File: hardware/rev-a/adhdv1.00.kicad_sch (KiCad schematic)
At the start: 0 parts

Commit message: Create power and MCU hierarchal pages
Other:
- added sheet MCU (mcu.kicad_sch)
- added sheet power (power.kicad_sch)
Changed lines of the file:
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@@
 	(generator_version "9.0")
 	(paper "A4")
+	(wire
+		(pts
+			(xy 135.89 38.1) (xy 135.89 39.37)
+		)
+		(stroke
+			(width 0)
+			(type default)
+		)
+	)
+	(sheet
+		(at 233.68 26.67)
+		(size 45.72 54.61)
+		(exclude_from_sim no)
+		(in_bom yes)
+		(on_board yes)
+		(dnp no)
+		(fields_autoplaced yes)
+		(stroke
+			(width 0.1524)
+			(type solid)
+		)
+		(fill
+			(color 0 0 0 0.0000)
+		)
+		(property "Sheetname" "MCU"
+			(at 233.68 25.9584 0)
+			(effects
+				(font
+					(size 1.27 1.27)
+				)
+				(justify left bottom)
+			)
+		)
+		(property "Sheetfile" "mcu.kicad_sch"
+			(at 233.68 81.8646 0)
+			(effects
+				(font
+					(size 1.27 1.27)
+				)
+				(justify left top)
+			)
+		)
+		(pin "GND" passive
+			(at 233.68 69.85 180)
+			(effects
+				(font
+					(size 1.27 1.27)
+				)
+				(justify left)
+			)
+		)
+		(pin "CHG_STAT" input
+			(at 233.68 43.18 180)
+			(effects
+				(font
+					(size 1.27 1.27)
+				)
+				(justify left)
+			)
+		)
+		(pin "3V3" input
+			(at 233.68 49.53 180)
+			(effects
+				(font
+					(size 1.27 1.27)
+				)
+				(justify left)
+			)
+		)
+		(pin "PGOOD_STAT" input
+			(at 233.68 57.15 180)
+			(effects
+				(font
+					(size 1.27 1.27)
+				)
+				(justify left)
+			)
+		)
+		(pin "VBAT_ADC" input
+			(at 233.68 36.83 180)
+			(effects
+				(font
+					(size 1.27 1.27)
+				)
+				(justify left)
+			)
+		)
+		(instances
+			(project "adhdv1.00"
+				(path "/13efd387-de04-4584-baa5-02298cbea49f"
+					(page "3")
+				)
+			)
+		)
+	)
+	(sheet
+		(at 135.89 26.67)
+		(size 90.17 54.61)
+		(exclude_from_sim no)
+		(in_bom yes)
+		(on_board yes)
+		(dnp no)
+		(fields_autoplaced yes)
+		(stroke
+			(width 0.1524)
+			(type solid)
+		)
+		(fill
+			(color 0 0 0 0.0000)
+		)
+		(property "Sheetname" "power"
+			(at 135.89 25.9584 0)
+			(effects
+				(font
+					(size 1.27 1.27)
+				)
+				(justify left bottom)
+			)
+		)
+		(property "Sheetfile" "power.kicad_sch"
+			(at 135.89 81.8646 0)
+			(effects
+				(font
+					(size 1.27 1.27)
+				)
+				(justify left top)
+			)
+		)
+		(pin "3V3" output
+			(at 226.06 49.53 0)
+			(effects
+				(font
+					(size 1.27 1.27)
+				)
+				(justify right)
+			)
+		)
+		(pin "GND" passive
+			(at 226.06 69.85 0)
+			(effects
+				(font
+					(size 1.27 1.27)
+				)
+				(justify right)
+			)
+		)
+		(pin "USB_5V" input
+			(at 135.89 39.37 180)
+			(effects
+				(font
+					(size 1.27 1.27)
+				)
+				(justify left)
+			)
+		)
+		(pin "VBAT" output
+			(at 135.89 58.42 180)
+			(effects
+				(font
+					(size 1.27 1.27)
+				)
+				(justify left)
+			)
+		)
+		(pin "VBAT_ADC" output
+			(at 226.06 36.83 0)
+			(effects
+				(font
+					(size 1.27 1.27)
+				)
+				(justify right)
+			)
+		)
+		(pin "CHG_STAT" output
+			(at 226.06 43.18 0)
+			(effects
+				(font
+					(size 1.27 1.27)
+				)
+				(justify right)
+			)
+		)
+		(pin "PGOOD_STAT" output
+			(at 226.06 57.15 0)
+			(effects
+				(font
+					(size 1.27 1.27)
+				)
+				(justify right)
+			)
+		)
+		(instances
+			(project "adhdv1.00"
+				(path "/13efd387-de04-4584-baa5-02298cbea49f"
+					(page "2")
+				)
+			)
+		)
+	)
 	(sheet_instances
 		(path "/"

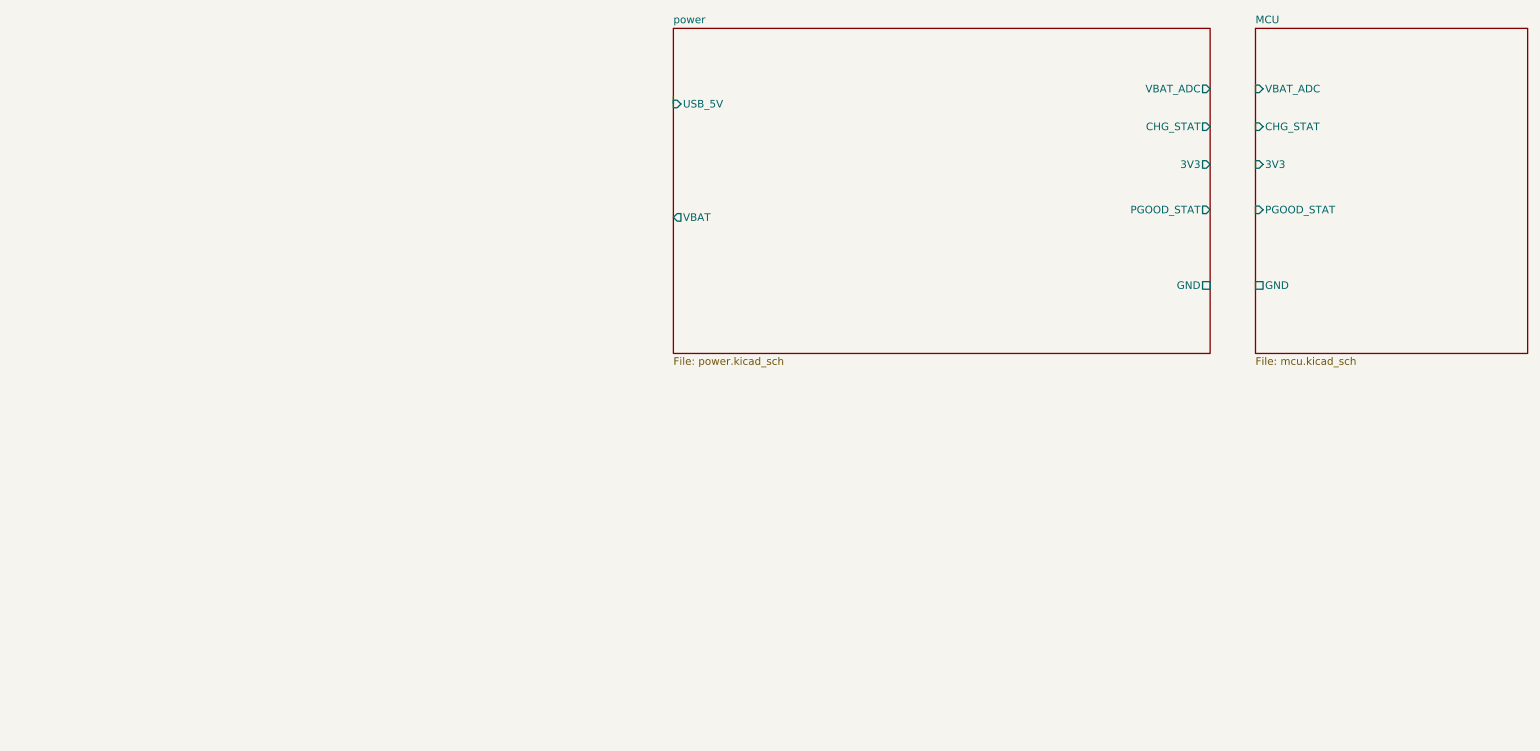
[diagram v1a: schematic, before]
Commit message: finalize MCU sheet and add haptic feedback sheet
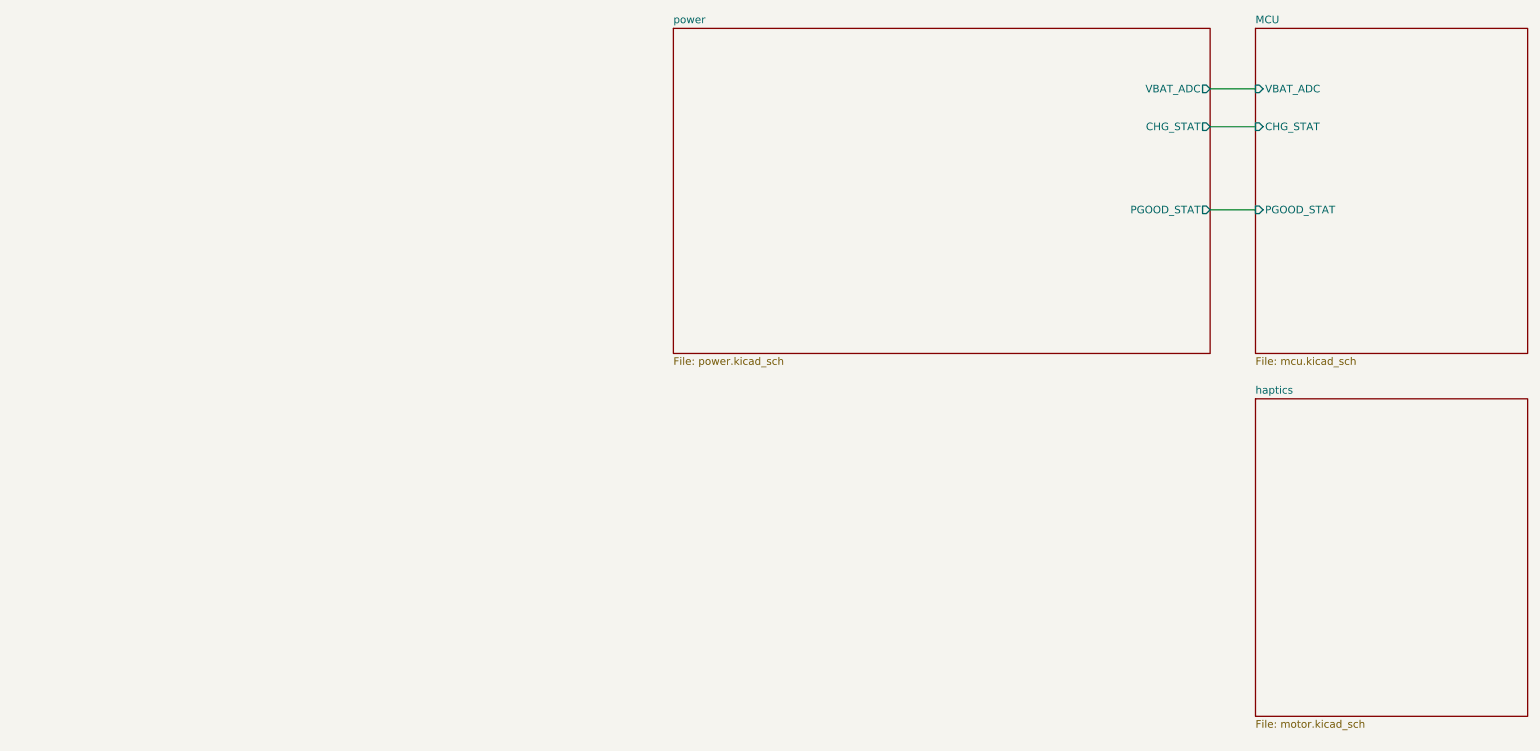
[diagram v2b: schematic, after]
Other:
- added sheet haptics (motor.kicad_sch)
- sheet MCU ports: added none; removed 3V3, GND
- sheet power ports: added none; removed 3V3, GND, USB_5V, VBAT
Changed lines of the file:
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@@
 	(wire
 		(pts
-			(xy 135.89 38.1) (xy 135.89 39.37)
+			(xy 226.06 57.15) (xy 233.68 57.15)
 		)
 		(stroke
 			(width 0)
 			(type default)
+		)
+	)
+	(wire
+		(pts
+			(xy 226.06 43.18) (xy 233.68 43.18)
+		)
+		(stroke
+			(width 0)
+			(type default)
+		)
+	)
+	(wire
+		(pts
+			(xy 226.06 36.83) (xy 233.68 36.83)
+		)
+		(stroke
+			(width 0)
+			(type default)
+		)
+	)
+	(sheet
+		(at 233.68 88.9)
+		(size 45.72 53.34)
+		(exclude_from_sim no)
+		(in_bom yes)
+		(on_board yes)
+		(dnp no)
+		(fields_autoplaced yes)
+		(stroke
+			(width 0.1524)
+			(type solid)
+		)
+		(fill
+			(color 0 0 0 0.0000)
+		)
+		(property "Sheetname" "haptics"
+			(at 233.68 88.1884 0)
+			(effects
+				(font
+					(size 1.27 1.27)
+				)
+				(justify left bottom)
+			)
+		)
+		(property "Sheetfile" "motor.kicad_sch"
+			(at 233.68 142.8246 0)
+			(effects
+				(font
+					(size 1.27 1.27)
+				)
+				(justify left top)
+			)
+		)
+		(instances
+			(project "adhdv1.00"
+				(path "/13efd387-de04-4584-baa5-02298cbea49f"
+					(page "4")
+				)
+			)
 		)
 	)
@@
 			)
 		)
-		(pin "GND" passive
-			(at 233.68 69.85 180)
-			(effects
-				(font
-					(size 1.27 1.27)
-				)
-				(justify left)
-			)
-		)
 		(pin "CHG_STAT" input
 			(at 233.68 43.18 180)
-			(effects
-				(font
-					(size 1.27 1.27)
-				)
-				(justify left)
-			)
-		)
-		(pin "3V3" input
-			(at 233.68 49.53 180)
 			(effects
 				(font
@@
 			)
 		)
-		(pin "3V3" output
-			(at 226.06 49.53 0)
-			(effects
-				(font
-					(size 1.27 1.27)
-				)
-				(justify right)
-			)
-		)
-		(pin "GND" passive
-			(at 226.06 69.85 0)
-			(effects
-				(font
-					(size 1.27 1.27)
-				)
-				(justify right)
-			)
-		)
-		(pin "USB_5V" input
-			(at 135.89 39.37 180)
-			(effects
-				(font
-					(size 1.27 1.27)
-				)
-				(justify left)
-			)
-		)
-		(pin "VBAT" output
-			(at 135.89 58.42 180)
-			(effects
-				(font
-					(size 1.27 1.27)
-				)
-				(justify left)
-			)
-		)

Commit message: Annotate schematic hierarchy and fix LED routing
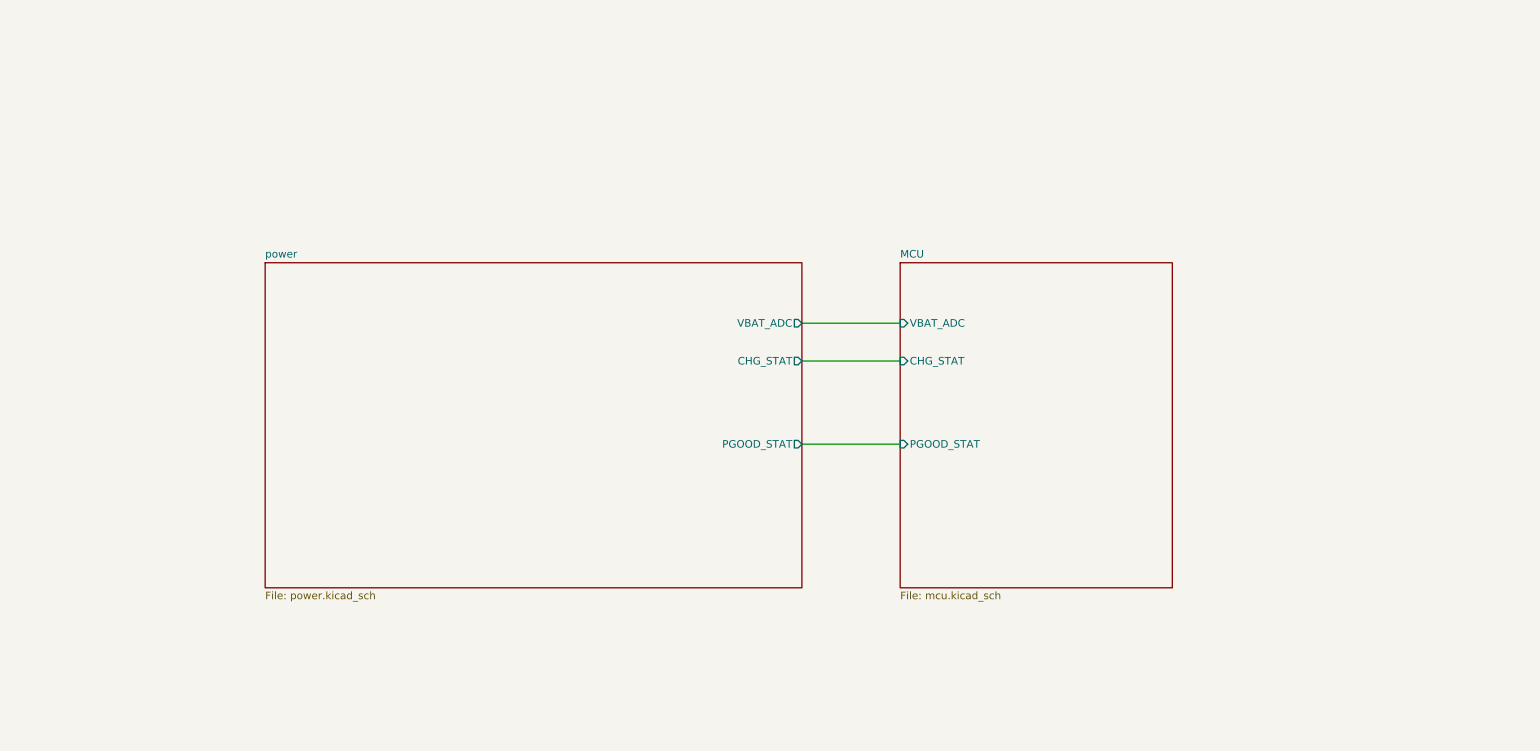
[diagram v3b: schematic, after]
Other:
- removed sheet haptics
- title: (none) -> ADHD MEDICATION REMINDER SYSTEM
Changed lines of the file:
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@@
 	(generator_version "9.0")
 	(paper "A4")
+	(title_block
+		(title "ADHD MEDICATION REMINDER SYSTEM")
+		(date "2026-03-8")
+		(rev "A")
+		(comment 1 "Designer: Maxwell Khor")
+	)
 	(wire
 		(pts
-			(xy 226.06 57.15) (xy 233.68 57.15)
+			(xy 157.48 96.52) (xy 173.99 96.52)
 		)
 		(stroke
@@
 	(wire
 		(pts
-			(xy 226.06 43.18) (xy 233.68 43.18)
+			(xy 157.48 82.55) (xy 173.99 82.55)
 		)
 		(stroke
@@
 	(wire
 		(pts
-			(xy 226.06 36.83) (xy 233.68 36.83)
+			(xy 157.48 76.2) (xy 173.99 76.2)
 		)
 		(stroke
@@
 	)
 	(sheet
-		(at 233.68 88.9)
-		(size 45.72 53.34)
-		(exclude_from_sim no)
-		(in_bom yes)
-		(on_board yes)
-		(dnp no)
-		(fields_autoplaced yes)
-		(stroke
-			(width 0.1524)
-			(type solid)
-		)
-		(fill
-			(color 0 0 0 0.0000)
-		)
-		(property "Sheetname" "haptics"
-			(at 233.68 88.1884 0)
-			(effects
-				(font
-					(size 1.27 1.27)
-				)
-				(justify left bottom)
-			)
-		)
-		(property "Sheetfile" "motor.kicad_sch"
-			(at 233.68 142.8246 0)
-			(effects
-				(font
-					(size 1.27 1.27)
-				)
-				(justify left top)
-			)
-		)
-		(instances
-			(project "adhdv1.00"
-				(path "/13efd387-de04-4584-baa5-02298cbea49f"
-					(page "4")
-				)
-			)
-		)
-	)
-	(sheet
-		(at 233.68 26.67)
+		(at 173.99 66.04)
 		(size 45.72 54.61)
 		(exclude_from_sim no)
@@
 		)
 		(property "Sheetname" "MCU"
-			(at 233.68 25.9584 0)
+			(at 173.99 65.3284 0)
 			(effects
 				(font
@@
 		)
 		(property "Sheetfile" "mcu.kicad_sch"
-			(at 233.68 81.8646 0)
+			(at 173.99 121.2346 0)
 			(effects
 				(font
@@
 		)
 		(pin "CHG_STAT" input
-			(at 233.68 43.18 180)
+			(at 173.99 82.55 180)
 			(effects
 				(font
@@
 		)
 		(pin "PGOOD_STAT" input
-			(at 233.68 57.15 180)
+			(at 173.99 96.52 180)
 			(effects
 				(font
@@
 		)
 		(pin "VBAT_ADC" input
-			(at 233.68 36.83 180)
+			(at 173.99 76.2 180)
 			(effects
 				(font
@@
 	)
 	(sheet
-		(at 135.89 26.67)
+		(at 67.31 66.04)
 		(size 90.17 54.61)
 		(exclude_from_sim no)
@@
 		)
 		(property "Sheetname" "power"
-			(at 135.89 25.9584 0)
+			(at 67.31 65.3284 0)
 			(effects
 				(font
@@
 		)
 		(property "Sheetfile" "power.kicad_sch"
-			(at 135.89 81.8646 0)
+			(at 67.31 121.2346 0)
 			(effects
 				(font
@@
 		)
 		(pin "VBAT_ADC" output
-			(at 226.06 36.83 0)
+			(at 157.48 76.2 0)
 			(effects
 				(font
@@
 		)
 		(pin "CHG_STAT" output
-			(at 226.06 43.18 0)
+			(at 157.48 82.55 0)
 			(effects
 				(font
@@
 		)
 		(pin "PGOOD_STAT" output
-			(at 226.06 57.15 0)
+			(at 157.48 96.52 0)
 			(effects
 				(font

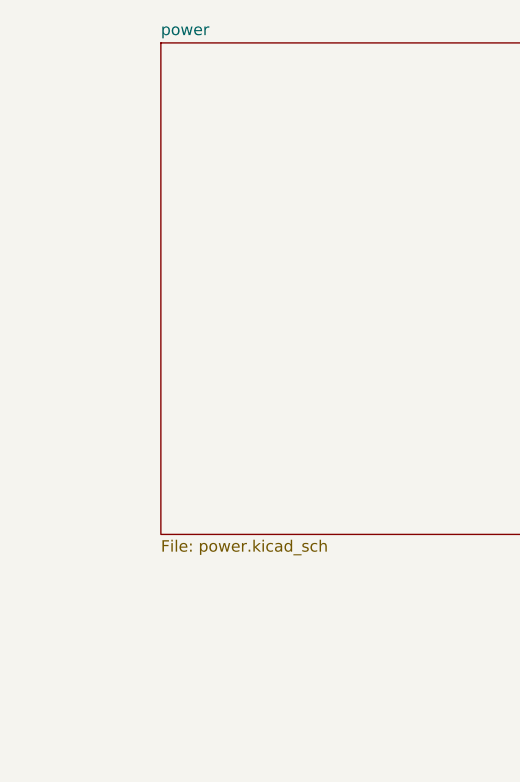
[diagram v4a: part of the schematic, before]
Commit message: Assign footprints and add additional bypass caps
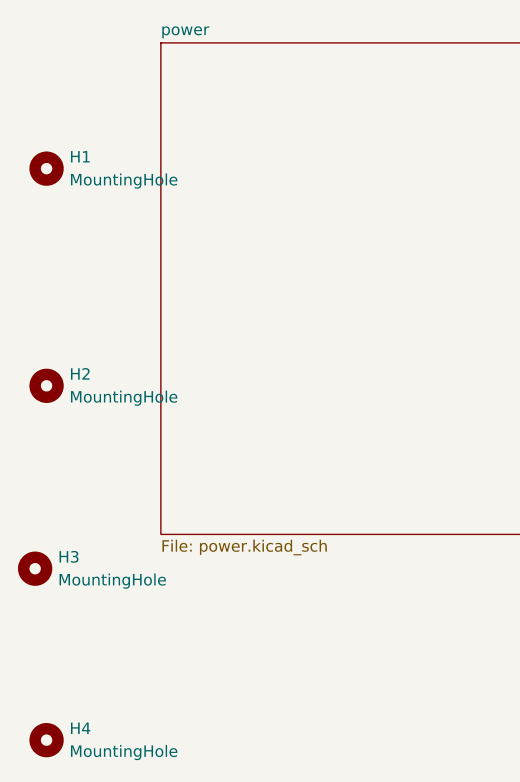
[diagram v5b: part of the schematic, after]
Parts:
- added H1, H2, H3, H4: MountingHole, MountingHole:MountingHole_2.2mm_M2_Pad, symbol Mechanical:MountingHole
